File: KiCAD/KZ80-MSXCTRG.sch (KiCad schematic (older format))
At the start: 29 parts, among them J1 MSX SLOT-A, J2 SBC8080 BUS, J3 SLT-JP, J4 Z80 CTRL, J5 PPI PORT-A, J6 SOUND, U1 74HC139, U2 74HC153, U3 74HC32, U4 74HC00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

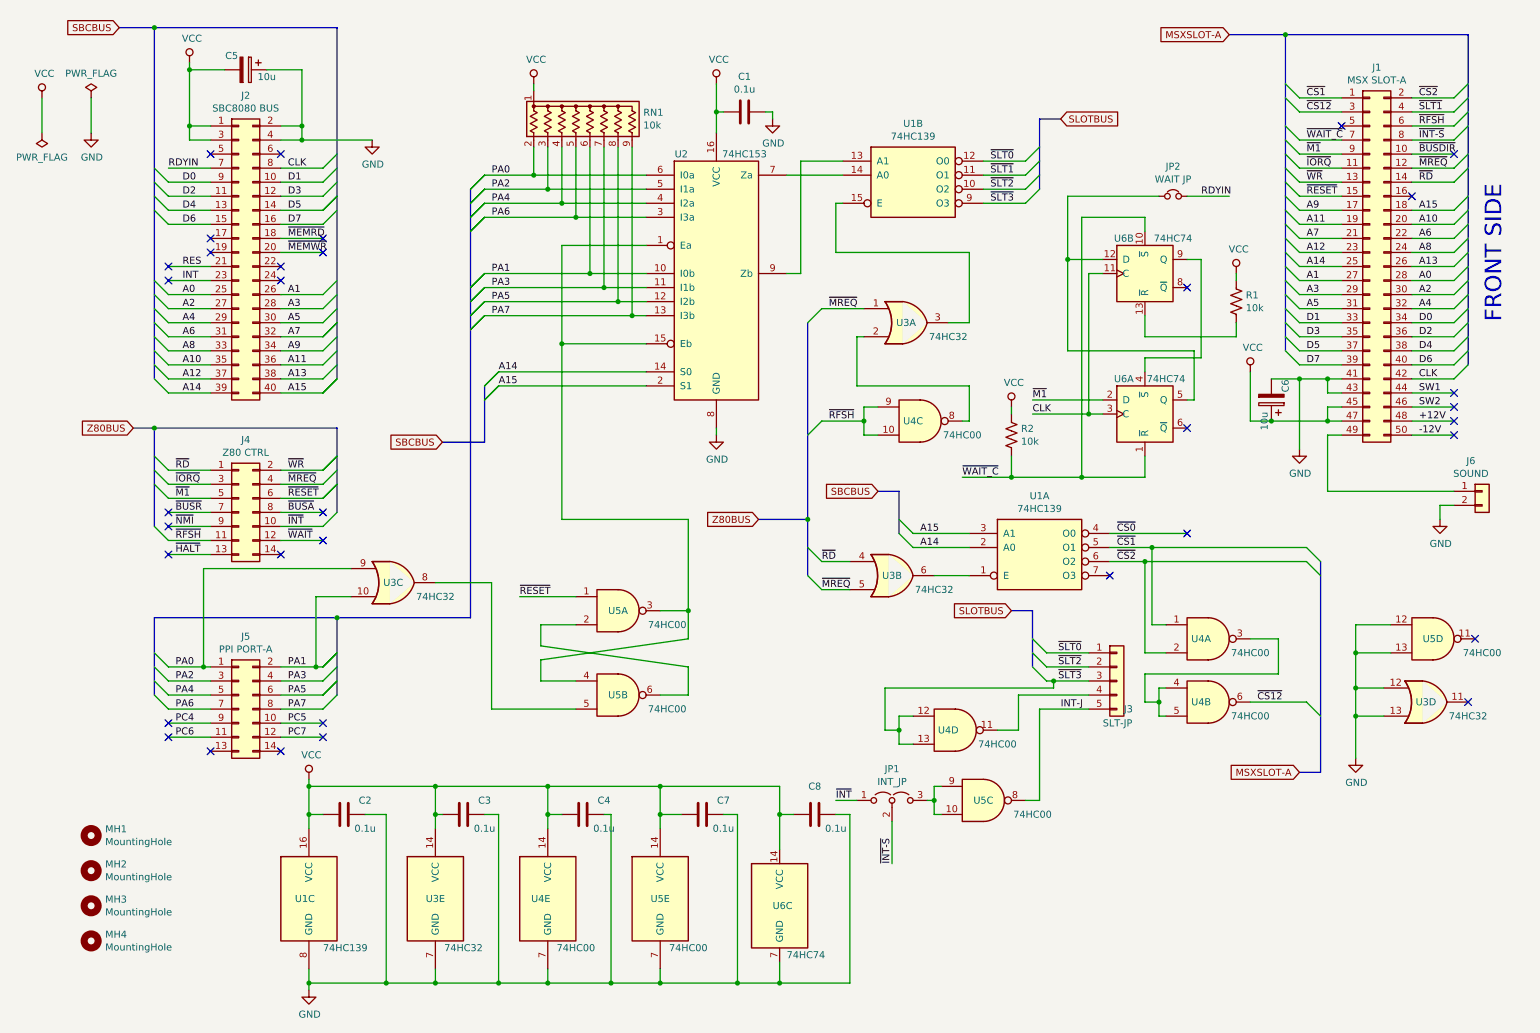
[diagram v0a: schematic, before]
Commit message: 2スロット対応
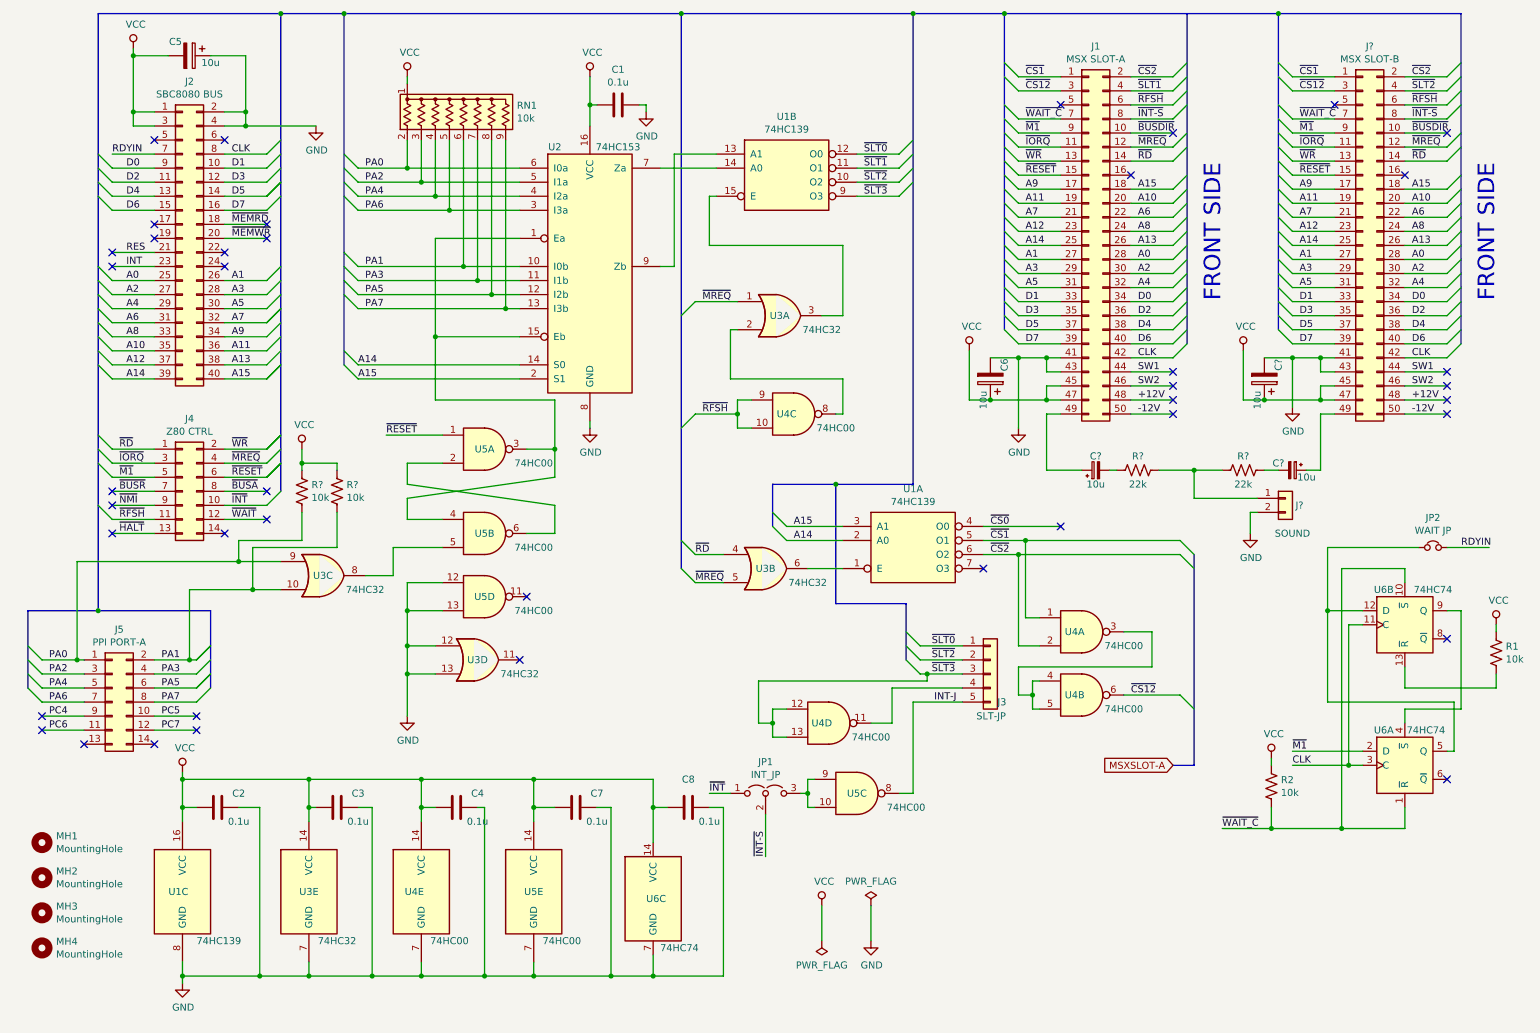
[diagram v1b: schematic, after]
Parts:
- removed J6: SOUND, Connector_PinHeader_2.54mm:PinHeader_1x02_P2.54mm_Horizontal, symbol Connector_Generic:Conn_01x02
- added C?: 10u, Capacitor_THT:CP_Radial_D5.0mm_P2.50mm, symbol Device:CP
- added C? (x2): 10u, symbol Device:CP_Small
- added J?: MSX SLOT-B, Connector_PinHeader_2.54mm:PCB_Edge_Conn_2x25_P2.54mm_Vertical, symbol Connector_Generic:Conn_02x25_Odd_Even
- added J?: SOUND, Connector_PinHeader_2.54mm:PinHeader_1x02_P2.54mm_Horizontal, symbol Connector_Generic:Conn_01x02
- added R? (x2): 22k, symbol Device:R_US
- added R? (x2): 10k, symbol Device:R_US
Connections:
- net +12V: now also J?.48 (Pin_48)
- net -12V: now also J?.50 (Pin_50)
- net A0: now also J?.28 (Pin_28)
- net A1: now also J?.27 (Pin_27)
- net A10: now also J?.20 (Pin_20)
- net A11: now also J?.19 (Pin_19)
- net A12: now also J?.23 (Pin_23)
- net A13: now also J?.26 (Pin_26)
- net A14: now also J?.25 (Pin_25)
- net A15: now also J?.18 (Pin_18)
- net A2: now also J?.30 (Pin_30)
- net A3: now also J?.29 (Pin_29)
- net A4: now also J?.32 (Pin_32)
- net A5: now also J?.31 (Pin_31)
- net A6: now also J?.22 (Pin_22)
- net A7: now also J?.21 (Pin_21)
- net A8: now also J?.24 (Pin_24)
- net A9: now also J?.17 (Pin_17)
- net CLK: now also J?.42 (Pin_42)
- net D0: now also J?.34 (Pin_34)
- net D1: now also J?.33 (Pin_33)
- net D2: now also J?.36 (Pin_36)
- net D3: now also J?.35 (Pin_35)
- net D4: now also J?.38 (Pin_38)
- net D5: now also J?.37 (Pin_37)
- net D6: now also J?.40 (Pin_40)
- net D7: now also J?.39 (Pin_39)
- net GND: now also C?.2, J?.2 (Pin_2), J?.41 (Pin_41), J?.43 (Pin_43)
- net PA0: now also R?.2
- net PA1: now also R?.2
- net SW1: now also J?.44 (Pin_44)
- net SW2: now also J?.46 (Pin_46)
- net VCC: now also C?.1, J?.45 (Pin_45), J?.47 (Pin_47), R?.1, R?.1
- net ~BUSDIR: now also J?.10 (Pin_10)
- net ~CS1: now also J?.1 (Pin_1)
- net ~CS12: now also J?.3 (Pin_3)
- net ~CS2: now also J?.2 (Pin_2)
- net ~INT-S: now also J?.8 (Pin_8)
- net ~IORQ: now also J?.11 (Pin_11)
- net ~M1: now also J?.9 (Pin_9)
- net ~MREQ: now also J?.12 (Pin_12)
- net ~RD: now also J?.14 (Pin_14)
- net ~RESET: now also J?.15 (Pin_15)
- net ~RFSH: now also J?.6 (Pin_6)
- net ~SLT2: now also J?.4 (Pin_4)
- net ~WAIT_C: now also J?.7 (Pin_7)
- net ~WR: now also J?.13 (Pin_13)
- net at J1.49 (Pin_49): now also C?.1
- new net: C?.1, J?.49 (Pin_49)
- new net: J?.1 (Pin_1), R?.1, R?.2
- new net: C?.2, R?.2
- new net: C?.2, R?.1
- no-connect marks 35 -> 42
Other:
- moved on the sheet: C1, C2, C3, C4, C5, C6, C7, C8, J1, J2, J3, J4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

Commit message: パターン改良ぬ
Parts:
- added R5: 10k, Resistor_THT:R_Axial_DIN0207_L6.3mm_D2.5mm_P10.16mm_Horizontal, symbol Device:R_US
- C11, C9: renamed from C?; footprint (none) -> Capacitor_THT:CP_Radial_D5.0mm_P2.50mm
- R3, R4, R6, R7: renamed from R?; footprint (none) -> Resistor_THT:R_Axial_DIN0207_L6.3mm_D2.5mm_P10.16mm_Horizontal
- gave numbers to parts that had none: 3
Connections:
- net VCC: now also R5.1
- net ~INT-S: now also R5.2
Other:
- moved on the sheet: J6
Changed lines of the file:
@@
 Title "KZ80 MSX ROM Cartridge Board"
 Date "2019-09-18"
-Rev "1"
+Rev "2"
 Comp "KUNI-NET"
 Comment1 ""
@@
 Entry Wire Line
 	5250 4550 5350 4650
-Text GLabel 8750 5950 0    50   Input ~ 0
-MSXSLOT-A
 Wire Wire Line
 	7400 4250 7950 4250
@@
 Connection ~ 7700 4350
 Wire Wire Line
-	7700 4350 8800 4350
+	7700 4350 8750 4350
 Wire Wire Line
 	7650 4450 7650 5100
@@
 Connection ~ 7650 4450
 Wire Wire Line
-	7650 4450 8800 4450
+	7650 4450 8750 4450
 Wire Wire Line
 	8400 5000 8600 5000
@@
 Connection ~ 7750 5450
 Wire Wire Line
-	8400 5450 8800 5450
+	8400 5450 8750 5450
 Text Label 8450 5450 0    50   ~ 0
 ~CS12
-Entry Wire Line
-	8900 4450 8800 4350
-Entry Wire Line
-	8900 4550 8800 4450
-Entry Wire Line
-	8900 5550 8800 5450
-Wire Bus Line
-	8750 5950 8900 5950
 NoConn ~ 7950 4250
 $Comp
@@
 $EndComp
 Wire Wire Line
-	5850 6300 5850 6600
-Text Label 5850 6600 1    50   ~ 0
+	5850 6300 5850 6550
+Text Label 5850 6900 1    50   ~ 0
 ~INT-S
 Wire Wire Line
@@
 Connection ~ 7550 600
 $Comp
-L Connector_Generic:Conn_02x25_Odd_Even J?
+L Connector_Generic:Conn_02x25_Odd_Even J7
 U 1 1 60694CA0
 P 10100 2250
-F 0 "J?" H 10150 3667 50  0000 C CNN
+F 0 "J7" H 10150 3667 50  0000 C CNN
 F 1 "MSX SLOT-B" H 10150 3576 50  0000 C CNN
 F 2 "Connector_PinHeader_2.54mm:PCB_Edge_Conn_2x25_P2.54mm_Vertical" H 10100 2250 50  0001 C CNN
@@
 D7
 $Comp
-L power:VCC #PWR?
+L power:VCC #PWR018
 U 1 1 60694D0D
 P 9250 3000
-F 0 "#PWR?" H 9250 2850 50  0001 C CNN
+F 0 "#PWR018" H 9250 2850 50  0001 C CNN
 F 1 "VCC" H 9267 3173 50  0000 C CNN
 F 2 "" H 9250 3000 50  0001 C CNN
@@
 $EndComp
 $Comp
-L power:GND #PWR?
+L power:GND #PWR019
 U 1 1 60694D13
 P 9600 3400
-F 0 "#PWR?" H 9600 3150 50  0001 C CNN
+F 0 "#PWR019" H 9600 3150 50  0001 C CNN
 F 1 "GND" H 9605 3227 50  0000 C CNN
 F 2 "" H 9600 3400 50  0001 C CNN
@@
 NoConn ~ 10700 1450
 $Comp
-L Device:CP C?
+L Device:CP C10
 U 1 1 60694D37
 P 9400 3200
-F 0 "C?" V 9300 3100 50  0000 C CNN
+F 0 "C10" V 9300 3100 50  0000 C CNN
 F 1 "10u" V 9450 3350 50  0000 C CNN
 F 2 "Capacitor_THT:CP_Radial_D5.0mm_P2.50mm" H 9438 3050 50  0001 C CNN
@@
 FRONT SIDE
 $Comp
-L Connector_Generic:Conn_01x02 J?
+L Connector_Generic:Conn_01x02 J6
 U 1 1 60694D49
-P 9550 4050
-F 0 "J?" H 9650 4000 50  0000 C CNN
-F 1 "SOUND" H 9600 3800 50  0000 C CNN
-F 2 "Connector_PinHeader_2.54mm:PinHeader_1x02_P2.54mm_Horizontal" H 9550 4050 50  0001 C CNN
-F 3 "~" H 9550 4050 50  0001 C CNN
-	1    9550 4050
+P 9650 4050
+F 0 "J6" H 9750 4000 50  0000 C CNN
+F 1 "SOUND" H 9700 3800 50  0000 C CNN
+F 2 "Connector_PinHeader_2.54mm:PinHeader_1x02_P2.54mm_Horizontal" H 9650 4050 50  0001 C CNN
+F 3 "~" H 9650 4050 50  0001 C CNN
+	1    9650 4050
 	1    0    0    -1
 $EndComp
@@
 L power:GND #PWR08
 U 1 1 5DA445DB
-P 9300 4300
-F 0 "#PWR08" H 9300 4050 50  0001 C CNN
-F 1 "GND" H 9305 4127 50  0000 C CNN
-F 2 "" H 9300 4300 50  0001 C CNN
-F 3 "" H 9300 4300 50  0001 C CNN
-	1    9300 4300
-	1    0    0    -1
-$EndComp
-Wire Wire Line
-	9300 4150 9350 4150
-Wire Wire Line
-	9300 4150 9300 4300
-$Comp
-L Device:CP_Small C?
+P 9400 4300
+F 0 "#PWR08" H 9400 4050 50  0001 C CNN
+F 1 "GND" H 9405 4127 50  0000 C CNN
+F 2 "" H 9400 4300 50  0001 C CNN
+F 3 "" H 9400 4300 50  0001 C CNN
+	1    9400 4300
+	1    0    0    -1
+$EndComp
+Wire Wire Line
+	9400 4150 9450 4150
+Wire Wire Line
+	9400 4150 9400 4300
+$Comp
+L Device:CP_Small C9
 U 1 1 6083400D
 P 8200 3850
-F 0 "C?" V 8300 3850 50  0000 C CNN
+F 0 "C9" V 8300 3850 50  0000 C CNN
 F 1 "10u" V 8100 3850 50  0000 C CNN
-F 2 "" H 8200 3850 50  0001 C CNN
+F 2 "Capacitor_THT:CP_Radial_D5.0mm_P2.50mm" H 8200 3850 50  0001 C CNN
 F 3 "~" H 8200 3850 50  0001 C CNN
 	1    8200 3850
@@
 $EndComp
 $Comp
-L Device:CP_Small C?
+L Device:CP_Small C11
 U 1 1 608355E2
 P 9600 3850
-F 0 "C?" V 9550 3750 50  0000 C CNN
+F 0 "C11" V 9550 3750 50  0000 C CNN
 F 1 "10u" V 9650 3950 50  0000 C CNN
-F 2 "" H 9600 3850 50  0001 C CNN
+F 2 "Capacitor_THT:CP_Radial_D5.0mm_P2.50mm" H 9600 3850 50  0001 C CNN
 F 3 "~" H 9600 3850 50  0001 C CNN
 	1    9600 3850
@@
 $EndComp
 $Comp
-L Device:R_US R?
+L Device:R_US R6
 U 1 1 60835DBB
 P 8500 3850
-F 0 "R?" V 8400 3850 50  0000 C CNN
+F 0 "R6" V 8400 3850 50  0000 C CNN
 F 1 "22k" V 8600 3850 50  0000 C CNN
-F 2 "" V 8540 3840 50  0001 C CNN
+F 2 "Resistor_THT:R_Axial_DIN0207_L6.3mm_D2.5mm_P10.16mm_Horizontal" V 8540 3840 50  0001 C CNN
 F 3 "~" H 8500 3850 50  0001 C CNN
 	1    8500 3850
@@
 $EndComp
 $Comp
-L Device:R_US R?
+L Device:R_US R7
 U 1 1 60837155
 P 9250 3850
-F 0 "R?" V 9150 3850 50  0000 C CNN
+F 0 "R7" V 9150 3850 50  0000 C CNN
 F 1 "22k" V 9350 3850 50  0000 C CNN
-F 2 "" V 9290 3840 50  0001 C CNN
+F 2 "Resistor_THT:R_Axial_DIN0207_L6.3mm_D2.5mm_P10.16mm_Horizontal" V 9290 3840 50  0001 C CNN
 F 3 "~" H 9250 3850 50  0001 C CNN
 	1    9250 3850
@@
 	9500 3850 9400 3850
 Wire Wire Line
-	8650 3850 8900 3850
-Wire Wire Line
 	8300 3850 8350 3850
 Wire Wire Line
-	8900 3850 8900 4050
-Wire Wire Line
-	8900 4050 9350 4050
-Connection ~ 8900 3850
-Wire Wire Line
-	8900 3850 9100 3850
+	9000 3850 9000 4050
+Wire Wire Line
+	9000 4050 9450 4050
 Wire Wire Line
 	6500 1800 6800 1800
@@
 $EndComp
 $Comp
-L Device:R_US R?
+L Device:R_US R3
 U 1 1 60ECC7BB
 P 2550 4000
-F 0 "R?" H 2618 4046 50  0000 L CNN
+F 0 "R3" H 2618 4046 50  0000 L CNN
 F 1 "10k" H 2618 3955 50  0000 L CNN
-F 2 "" V 2590 3990 50  0001 C CNN
+F 2 "Resistor_THT:R_Axial_DIN0207_L6.3mm_D2.5mm_P10.16mm_Horizontal" V 2590 3990 50  0001 C CNN
 F 3 "~" H 2550 4000 50  0001 C CNN
 	1    2550 4000
@@
 $EndComp
 $Comp
-L Device:R_US R?
+L Device:R_US R4
 U 1 1 60ECCAF1
 P 2800 4000
-F 0 "R?" H 2868 4046 50  0000 L CNN
+F 0 "R4" H 2868 4046 50  0000 L CNN
 F 1 "10k" H 2868 3955 50  0000 L CNN
-F 2 "" V 2840 3990 50  0001 C CNN
+F 2 "Resistor_THT:R_Axial_DIN0207_L6.3mm_D2.5mm_P10.16mm_Horizontal" V 2840 3990 50  0001 C CNN
 F 3 "~" H 2800 4000 50  0001 C CNN
 	1    2800 4000
@@
 	2200 4700 2400 4700
 $Comp
-L power:VCC #PWR?
+L power:VCC #PWR016
 U 1 1 60F3696F
 P 2550 3700
-F 0 "#PWR?" H 2550 3550 50  0001 C CNN
+F 0 "#PWR016" H 2550 3550 50  0001 C CNN
 F 1 "VCC" H 2567 3873 50  0000 C CNN
 F 2 "" H 2550 3700 50  0001 C CNN
@@
 Wire Bus Line
 	6350 4800 6850 4800
+Connection ~ 6350 3950
+Wire Bus Line
+	6350 3950 6900 3950
+Connection ~ 9000 3850
+Wire Wire Line
+	9000 3850 9100 3850
+Wire Wire Line
+	8650 3850 9000 3850
+Entry Wire Line
+	8750 5450 8850 5350
+Entry Wire Line
+	8750 4450 8850 4350
+Entry Wire Line
+	8750 4350 8850 4250
+$Comp
+L Device:R_US R5
+U 1 1 60418799
+P 6050 6550
+F 0 "R5" V 5845 6550 50  0000 C CNN
+F 1 "10k" V 5936 6550 50  0000 C CNN
+F 2 "Resistor_THT:R_Axial_DIN0207_L6.3mm_D2.5mm_P10.16mm_Horizontal" V 6090 6540 50  0001 C CNN
+F 3 "~" H 6050 6550 50  0001 C CNN
+	1    6050 6550
+	0    1    1    0
+$EndComp
+Wire Wire Line
+	5850 6550 5900 6550
+Connection ~ 5850 6550
+Wire Wire Line
+	5850 6550 5850 6900
+$Comp
+L power:VCC #PWR017
+U 1 1 604BF23B
+P 6250 6500
+F 0 "#PWR017" H 6250 6350 50  0001 C CNN
+F 1 "VCC" H 6267 6673 50  0000 C CNN
+F 2 "" H 6250 6500 50  0001 C CNN
+F 3 "" H 6250 6500 50  0001 C CNN
+	1    6250 6500
+	1    0    0    -1
+$EndComp
+Wire Wire Line
+	6250 6500 6250 6550
+Wire Wire Line
+	6250 6550 6200 6550
 Wire Bus Line
 	5900 3950 5900 4250
@@
 	6850 4800 6850 5200
 Wire Bus Line
-	8900 4450 8900 5950
-Wire Bus Line
 	5250 600  5250 4550
 Wire Bus Line
@@
 	7550 600  7550 2850
 Wire Bus Line
-	8850 600  8850 2950
-Wire Bus Line
 	1100 600  1100 4850
-Connection ~ 6350 3950
-Wire Bus Line
-	6350 3950 6900 3950
+Wire Bus Line
+	8850 600  8850 5350
 $EndSCHEMATC
